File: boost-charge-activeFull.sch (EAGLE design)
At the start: 20 parts, among them U1 MCP73831

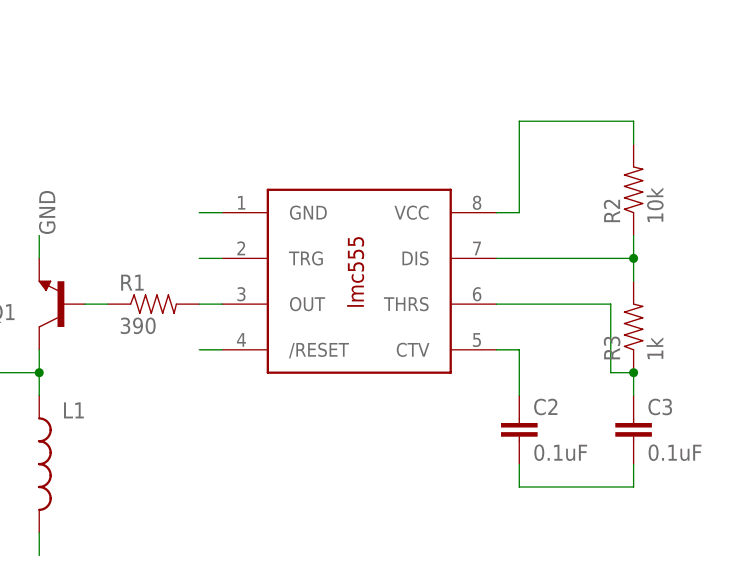
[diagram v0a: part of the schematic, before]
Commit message: Connected trigger
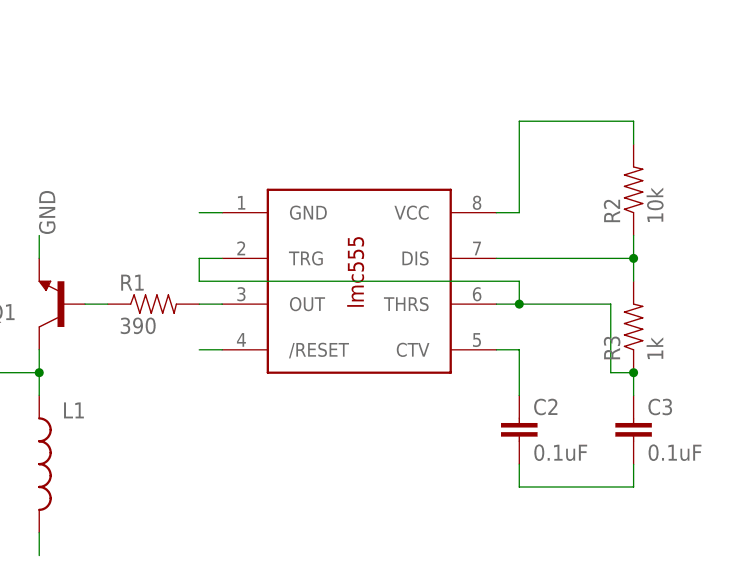
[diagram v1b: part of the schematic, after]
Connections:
- removed net N$6: C3.1, R3.1, U$1.THRS
- net N$5: now also C3.1, R3.1, U$1.THRS
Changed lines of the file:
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@@
 <pinref part="U$1" gate="G$1" pin="TRG"/>
 <wire x1="55.88" y1="38.1" x2="53.34" y2="38.1" width="0.1524" layer="91"/>
-</segment>
-</net>
-<net name="N$6" class="0">
-<segment>
+<wire x1="53.34" y1="38.1" x2="53.34" y2="35.56" width="0.1524" layer="91"/>
 <pinref part="U$1" gate="G$1" pin="THRS"/>
-<wire x1="86.36" y1="33.02" x2="99.06" y2="33.02" width="0.1524" layer="91"/>
+<wire x1="86.36" y1="33.02" x2="88.9" y2="33.02" width="0.1524" layer="91"/>
+<wire x1="88.9" y1="33.02" x2="99.06" y2="33.02" width="0.1524" layer="91"/>
 <wire x1="99.06" y1="33.02" x2="99.06" y2="25.4" width="0.1524" layer="91"/>
 <pinref part="R3" gate="G$1" pin="1"/>
@@
 <junction x="101.6" y="25.4"/>
 <pinref part="C3" gate="G$1" pin="1"/>
+<wire x1="53.34" y1="35.56" x2="88.9" y2="35.56" width="0.1524" layer="91"/>
+<wire x1="88.9" y1="35.56" x2="88.9" y2="33.02" width="0.1524" layer="91"/>
+<junction x="88.9" y="33.02"/>
 </segment>
 </net>
